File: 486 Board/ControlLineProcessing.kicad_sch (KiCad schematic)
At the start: 16 parts, among them U2 7404, U3 7400, U4 74138, U5 74244, U6 7408, U7 7400, U8 74244, U9 74139

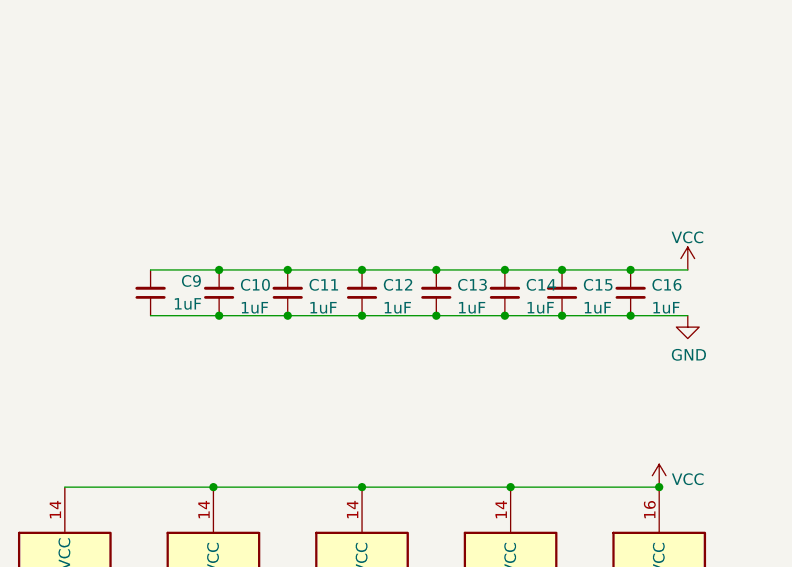
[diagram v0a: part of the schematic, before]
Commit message: * Layout Template for eurocard format * 486 Board updated to new layout * Support board draft * Added 6u eurocard backplane meant for ATX case
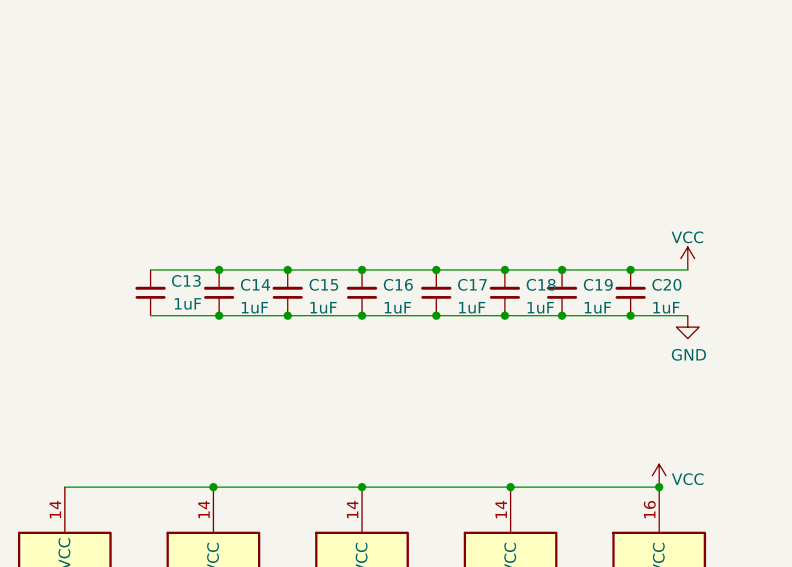
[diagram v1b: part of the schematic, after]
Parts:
- renumbered C9 to C13, C10 to C14, C11 to C15, C12 to C16, C13 to C17, C14 to C18, C15 to C19, C16 to C20
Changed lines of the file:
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@@
   (symbol (lib_id "power:VCC") (at 41.275 17.78 0) (unit 1)
     (in_bom yes) (on_board yes) (fields_autoplaced)
-    (property "Reference" "#PWR029" (id 0) (at 41.275 21.59 0)
+    (property "Reference" "#PWR023" (id 0) (at 41.275 21.59 0)
       (effects (font (size 1.27 1.27)) hide)
     )
@@
   (symbol (lib_id "Device:C_Small") (at 205.105 67.31 180) (unit 1)
     (in_bom yes) (on_board yes) (fields_autoplaced)
-    (property "Reference" "C10" (id 0) (at 207.4291 66.4689 0)
+    (property "Reference" "C14" (id 0) (at 207.4291 66.4689 0)
       (effects (font (size 1.27 1.27)) (justify right))
     )
@@
   (symbol (lib_id "Device:C_Small") (at 236.855 67.31 180) (unit 1)
     (in_bom yes) (on_board yes) (fields_autoplaced)
-    (property "Reference" "C14" (id 0) (at 239.1791 66.4689 0)
+    (property "Reference" "C18" (id 0) (at 239.1791 66.4689 0)
       (effects (font (size 1.27 1.27)) (justify right))
     )
@@
   (symbol (lib_id "power:VCC") (at 254 88.9 0) (unit 1)
     (in_bom yes) (on_board yes) (fields_autoplaced)
-    (property "Reference" "#PWR036" (id 0) (at 254 92.71 0)
+    (property "Reference" "#PWR030" (id 0) (at 254 92.71 0)
       (effects (font (size 1.27 1.27)) hide)
     )
@@
   (symbol (lib_id "power:GND") (at 81.28 121.92 0) (mirror y) (unit 1)
     (in_bom yes) (on_board yes)
-    (property "Reference" "#PWR033" (id 0) (at 81.28 128.27 0)
+    (property "Reference" "#PWR027" (id 0) (at 81.28 128.27 0)
       (effects (font (size 1.27 1.27)) hide)
     )
@@
   (symbol (lib_id "Device:C_Small") (at 229.235 67.31 180) (unit 1)
     (in_bom yes) (on_board yes) (fields_autoplaced)
-    (property "Reference" "C13" (id 0) (at 231.5591 66.4689 0)
+    (property "Reference" "C17" (id 0) (at 231.5591 66.4689 0)
       (effects (font (size 1.27 1.27)) (justify right))
     )
@@
   (symbol (lib_id "power:GND") (at 106.045 142.24 0) (mirror y) (unit 1)
     (in_bom yes) (on_board yes)
-    (property "Reference" "#PWR035" (id 0) (at 106.045 148.59 0)
+    (property "Reference" "#PWR029" (id 0) (at 106.045 148.59 0)
       (effects (font (size 1.27 1.27)) hide)
     )
@@
   (symbol (lib_id "power:GND") (at 257.175 69.85 0) (unit 1)
     (in_bom yes) (on_board yes)
-    (property "Reference" "#PWR039" (id 0) (at 257.175 76.2 0)
+    (property "Reference" "#PWR033" (id 0) (at 257.175 76.2 0)
       (effects (font (size 1.27 1.27)) hide)
     )
@@
   (symbol (lib_id "Device:C_Small") (at 243.205 67.31 180) (unit 1)
     (in_bom yes) (on_board yes) (fields_autoplaced)
-    (property "Reference" "C15" (id 0) (at 245.5291 66.4689 0)
+    (property "Reference" "C19" (id 0) (at 245.5291 66.4689 0)
       (effects (font (size 1.27 1.27)) (justify right))
     )
@@
   (symbol (lib_id "power:VCC") (at 106.045 101.6 0) (unit 1)
     (in_bom yes) (on_board yes) (fields_autoplaced)
-    (property "Reference" "#PWR034" (id 0) (at 106.045 105.41 0)
+    (property "Reference" "#PWR028" (id 0) (at 106.045 105.41 0)
       (effects (font (size 1.27 1.27)) hide)
     )
@@
   (symbol (lib_id "power:VCC") (at 257.175 64.77 0) (unit 1)
     (in_bom yes) (on_board yes) (fields_autoplaced)
-    (property "Reference" "#PWR038" (id 0) (at 257.175 68.58 0)
+    (property "Reference" "#PWR032" (id 0) (at 257.175 68.58 0)
       (effects (font (size 1.27 1.27)) hide)
     )
@@
   (symbol (lib_id "power:GND") (at 41.275 53.34 0) (mirror y) (unit 1)
     (in_bom yes) (on_board yes)
-    (property "Reference" "#PWR030" (id 0) (at 41.275 59.69 0)
+    (property "Reference" "#PWR024" (id 0) (at 41.275 59.69 0)
       (effects (font (size 1.27 1.27)) hide)
     )
@@
   (symbol (lib_id "power:GND") (at 254 114.3 0) (mirror y) (unit 1)
     (in_bom yes) (on_board yes)
-    (property "Reference" "#PWR037" (id 0) (at 254 120.65 0)
+    (property "Reference" "#PWR031" (id 0) (at 254 120.65 0)
       (effects (font (size 1.27 1.27)) hide)
     )
@@
   (symbol (lib_id "Device:C_Small") (at 250.825 67.31 180) (unit 1)
     (in_bom yes) (on_board yes) (fields_autoplaced)
-    (property "Reference" "C16" (id 0) (at 253.1491 66.4689 0)
+    (property "Reference" "C20" (id 0) (at 253.1491 66.4689 0)
       (effects (font (size 1.27 1.27)) (justify right))
     )
@@
   (symbol (lib_id "Device:C_Small") (at 220.98 67.31 180) (unit 1)
     (in_bom yes) (on_board yes) (fields_autoplaced)
-    (property "Reference" "C12" (id 0) (at 223.3041 66.4689 0)
+    (property "Reference" "C16" (id 0) (at 223.3041 66.4689 0)
       (effects (font (size 1.27 1.27)) (justify right))
     )
@@
   (symbol (lib_id "power:VCC") (at 44.45 64.77 0) (unit 1)
     (in_bom yes) (on_board yes) (fields_autoplaced)
-    (property "Reference" "#PWR031" (id 0) (at 44.45 68.58 0)
+    (property "Reference" "#PWR025" (id 0) (at 44.45 68.58 0)
       (effects (font (size 1.27 1.27)) hide)
     )
@@
   (symbol (lib_id "Device:C_Small") (at 212.725 67.31 180) (unit 1)
     (in_bom yes) (on_board yes) (fields_autoplaced)
-    (property "Reference" "C11" (id 0) (at 215.0491 66.4689 0)
+    (property "Reference" "C15" (id 0) (at 215.0491 66.4689 0)
       (effects (font (size 1.27 1.27)) (justify right))
     )
@@
   (symbol (lib_id "Device:C_Small") (at 197.485 67.31 180) (unit 1)
     (in_bom yes) (on_board yes)
-    (property "Reference" "C9" (id 0) (at 203.2 66.04 0)
+    (property "Reference" "C13" (id 0) (at 203.2 66.04 0)
       (effects (font (size 1.27 1.27)) (justify left))
     )
@@
   (symbol (lib_id "power:GND") (at 44.45 105.41 0) (mirror y) (unit 1)
     (in_bom yes) (on_board yes)
-    (property "Reference" "#PWR032" (id 0) (at 44.45 111.76 0)
-      (effects (font (size 1.27 1.27)) hide)
-    )
+    (property "Reference" "#PWR026" (id 0) (at 44.45 111.76 0)
+      (effects (font (size 1.27 1.27)) hide)
+    )
